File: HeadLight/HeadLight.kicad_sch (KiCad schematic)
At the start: 23 parts

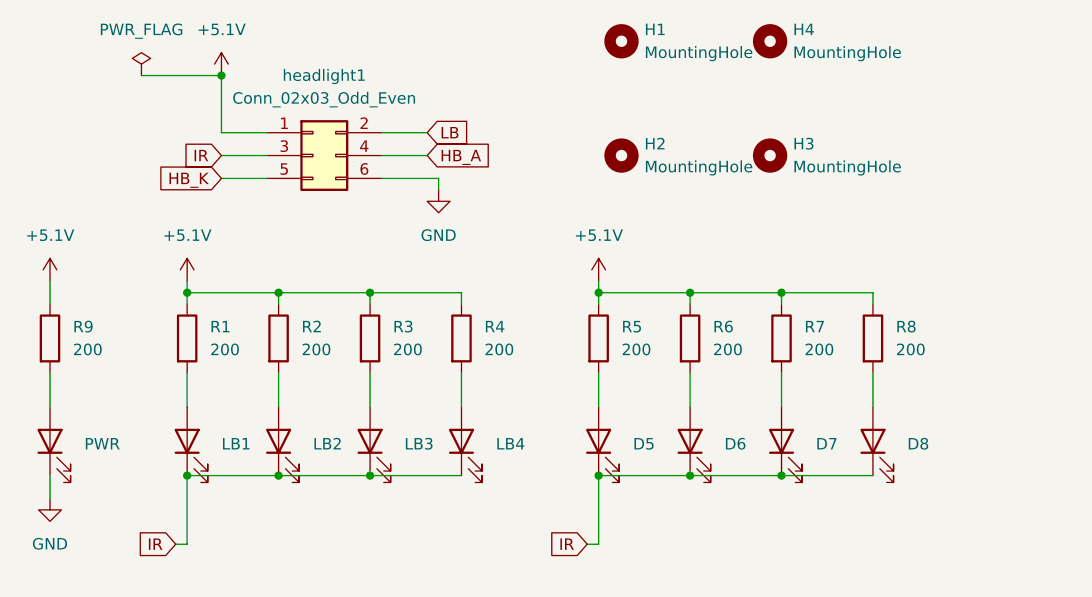
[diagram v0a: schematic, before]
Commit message: 基板防水(LAN)作成開始
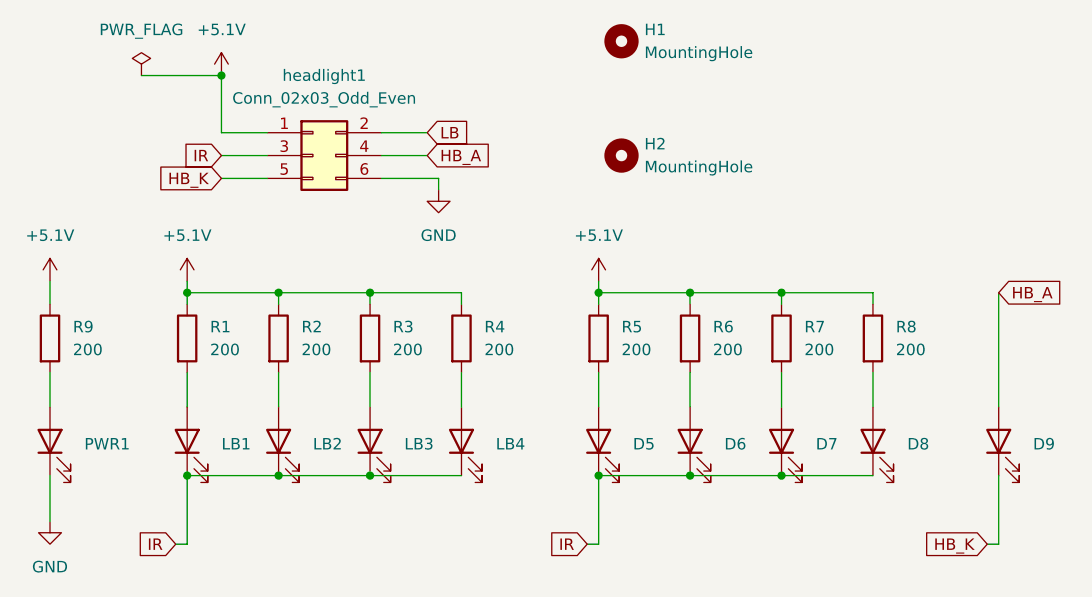
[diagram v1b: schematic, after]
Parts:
- removed H3, H4: MountingHole, symbol Mechanical:MountingHole
- added D9: LED, basic_parts:power led, symbol Device:LED
- H1, H2: footprint (none) -> MountingHole:MountingHole_3.2mm_M3
- renumbered PWR to PWR1
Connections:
- net HB_A: now also D9.2 (A)
- net HB_K: now also D9.1 (K)
